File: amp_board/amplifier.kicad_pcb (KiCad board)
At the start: 2 copper layers, 148.6 x 171.4 mm, 81 parts, among them J1 AUDIO_IN, J2 +VDC, J3 COM, J4 -VDC, J5 OUT_CTL, J6 SPK_POS, J7 SPK_NEG, Q1 BC846, Q10 BC850, Q11 2SK135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

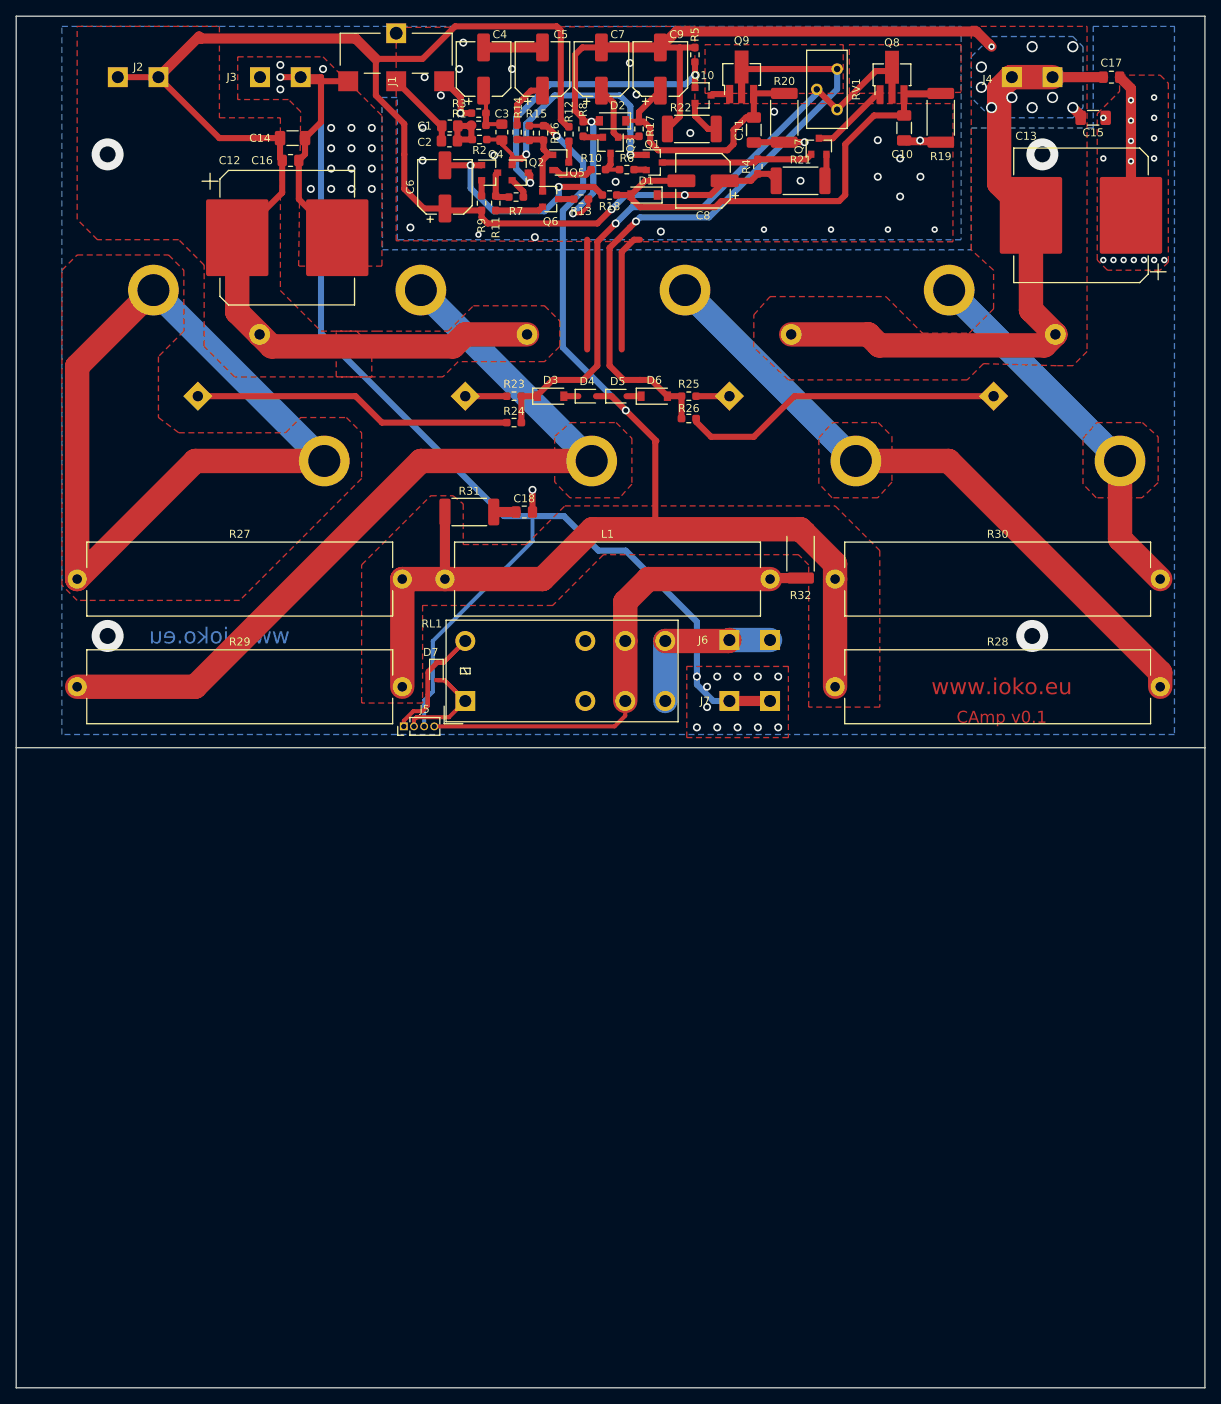
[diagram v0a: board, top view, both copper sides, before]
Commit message: update xformer soft startup
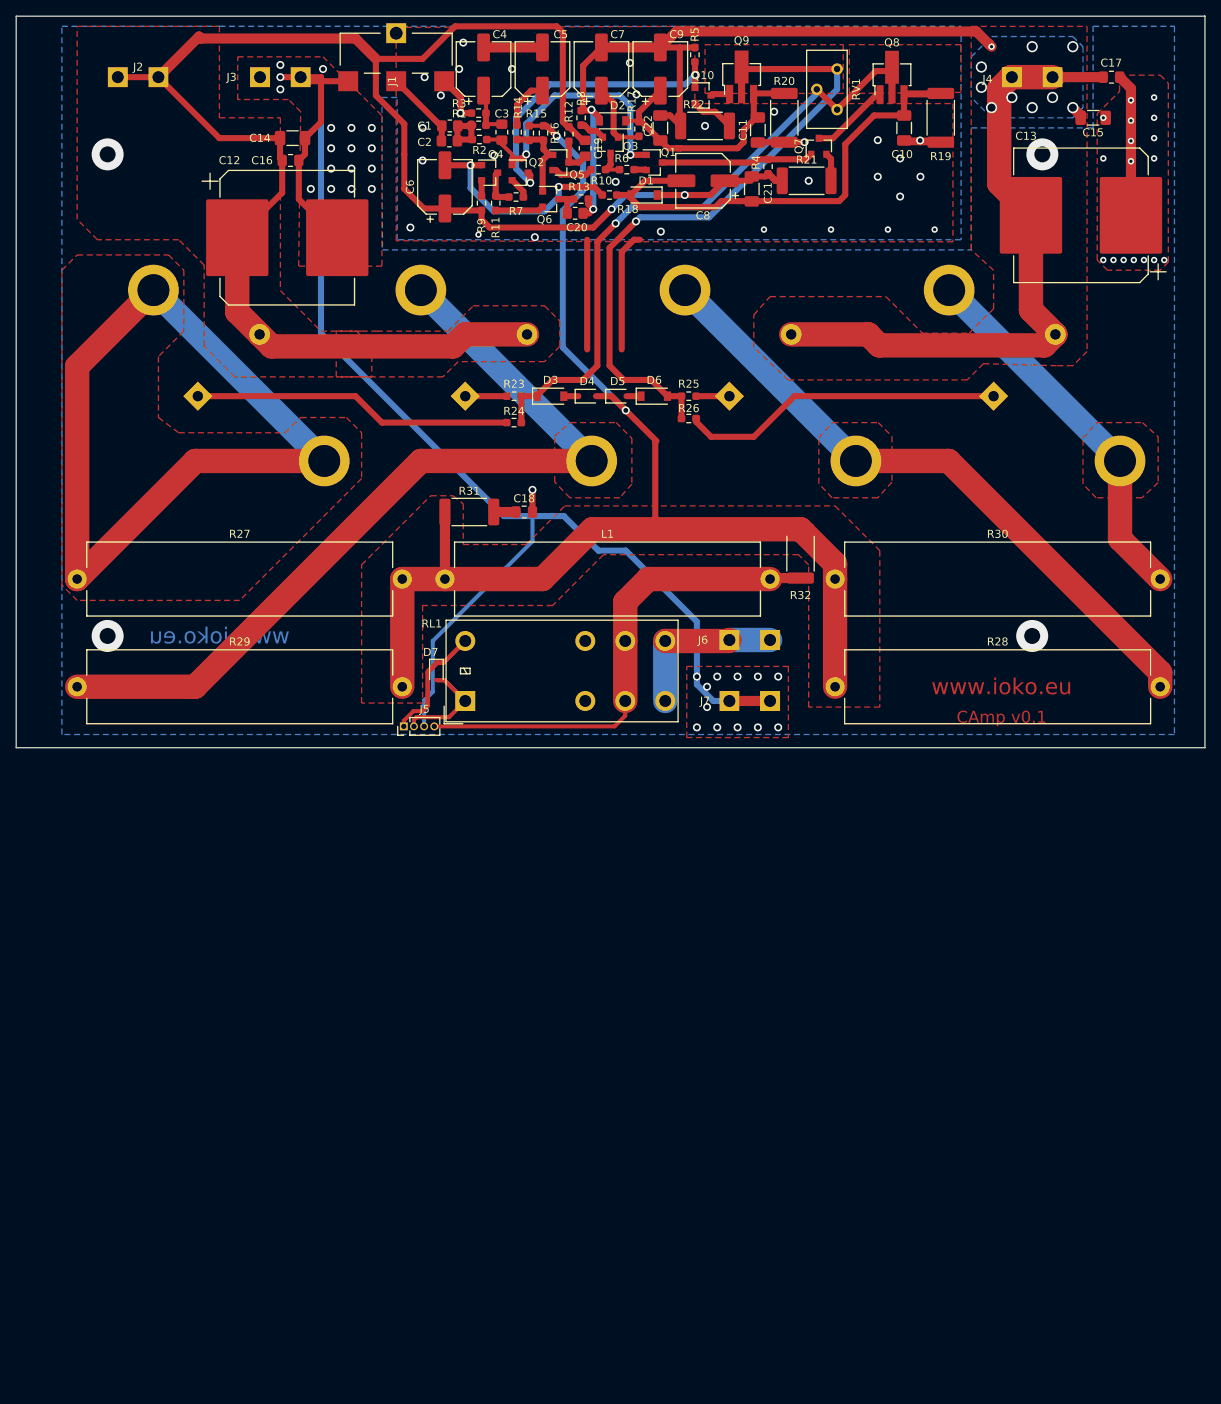
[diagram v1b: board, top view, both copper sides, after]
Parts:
- added C19: 22pF, Resistor_SMD:R_0805_2012Metric_Pad1.20x1.40mm_HandSolder, F.Cu at (94.2, 35.6)
- added C20: 22pF, Resistor_SMD:R_0805_2012Metric_Pad1.20x1.40mm_HandSolder, F.Cu at (93.0, 43.7)
- added C21: 330nF, Capacitor_SMD:C_1206_3216Metric_Pad1.33x1.80mm_HandSolder, F.Cu at (115.1, 40.6)
- added C22: 330nF, Capacitor_SMD:C_1206_3216Metric_Pad1.33x1.80mm_HandSolder, F.Cu at (103.6, 33.0)
- moved R22 1.69 mm to (109.2, 32.8)
- moved R8 1.42 mm to (93.7, 31.8)
- moved R4 1.27 mm to (117.1, 37.8)
- moved R21 0.76 mm to (121.9, 39.6)
- moved C11 0.51 mm to (115.8, 33.3)
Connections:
- RL1 pad 2: (no net) -> Net-(RL1-Pad2)
- RL1 pad 7: (no net) -> Net-(RL1-Pad7)
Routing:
- net +VDC: track 227.1 -> 232.1 mm
- net Net-(C19-Pad2): track 2.65 -> 5.02 mm
- net Net-(C20-Pad1): track 1.90 -> 3.77 mm
- net -VDC: track 178.9 -> 177.1 mm
- net Net-(Q3-Pad2): track 2.53 -> 3.36 mm
- net Net-(Q10-Pad2): track 4.94 -> 5.54 mm
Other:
- board size 148.6 x 171.4 mm -> 148.6 x 91.4 mm
